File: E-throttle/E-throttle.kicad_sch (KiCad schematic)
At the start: 68 parts, among them IC1 BTS441TG, J1 Conn_01x15_Socket, J2 Conn_01x15_Socket, J3 Conn_01x11, J4 Conn_01x11, J5 776087-1, J9 Micro_SD_Card, Q1 NMOS, SW1 SW_Push, U1 74HC123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

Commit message: Changed Stepper motor driver headers to female headers
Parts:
- J3, J4: footprint Connector_PinHeader_2.54mm:PinHeader_1x11_P2.54mm_Vertical -> Connector_PinSocket_2.54mm:PinSocket_1x11_P2.54mm_Vertical

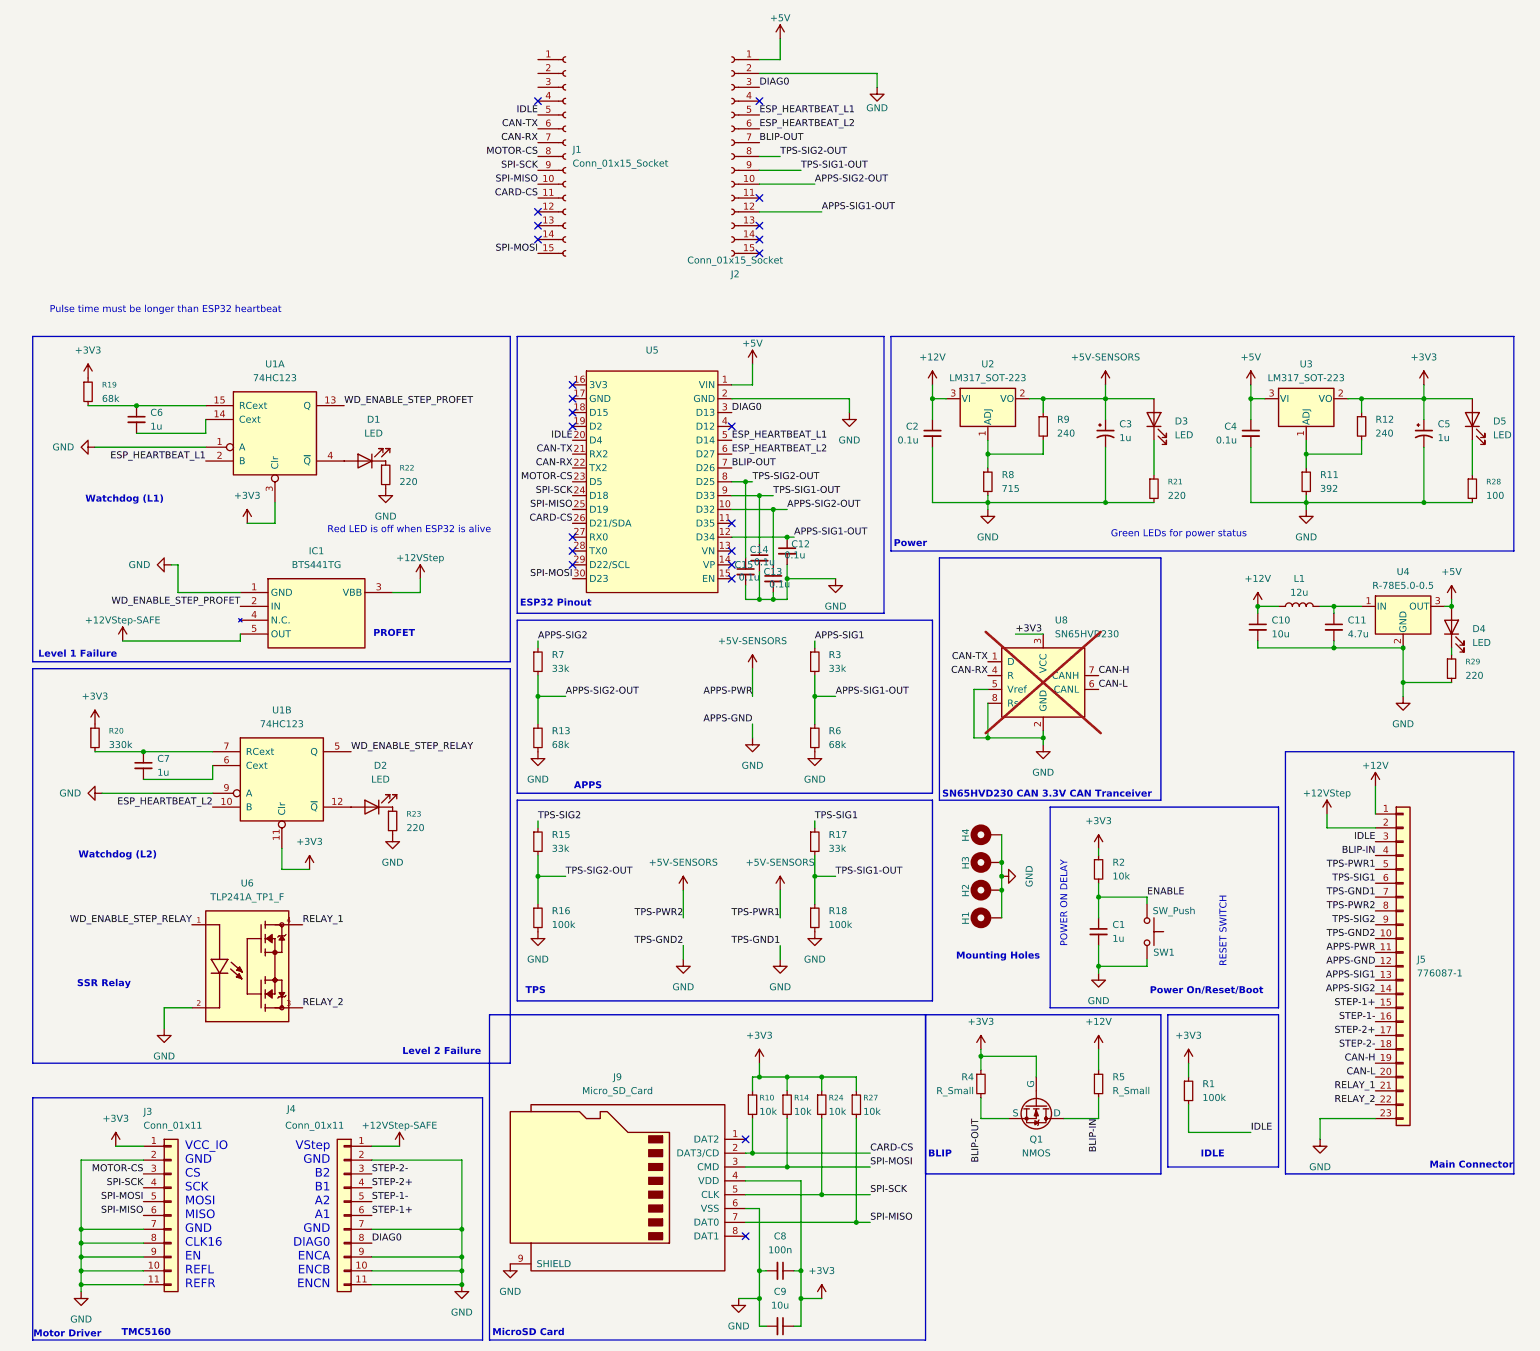
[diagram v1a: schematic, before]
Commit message: Deleted IDLE Control circuit
Fully disconnected IDLE control pin from loom
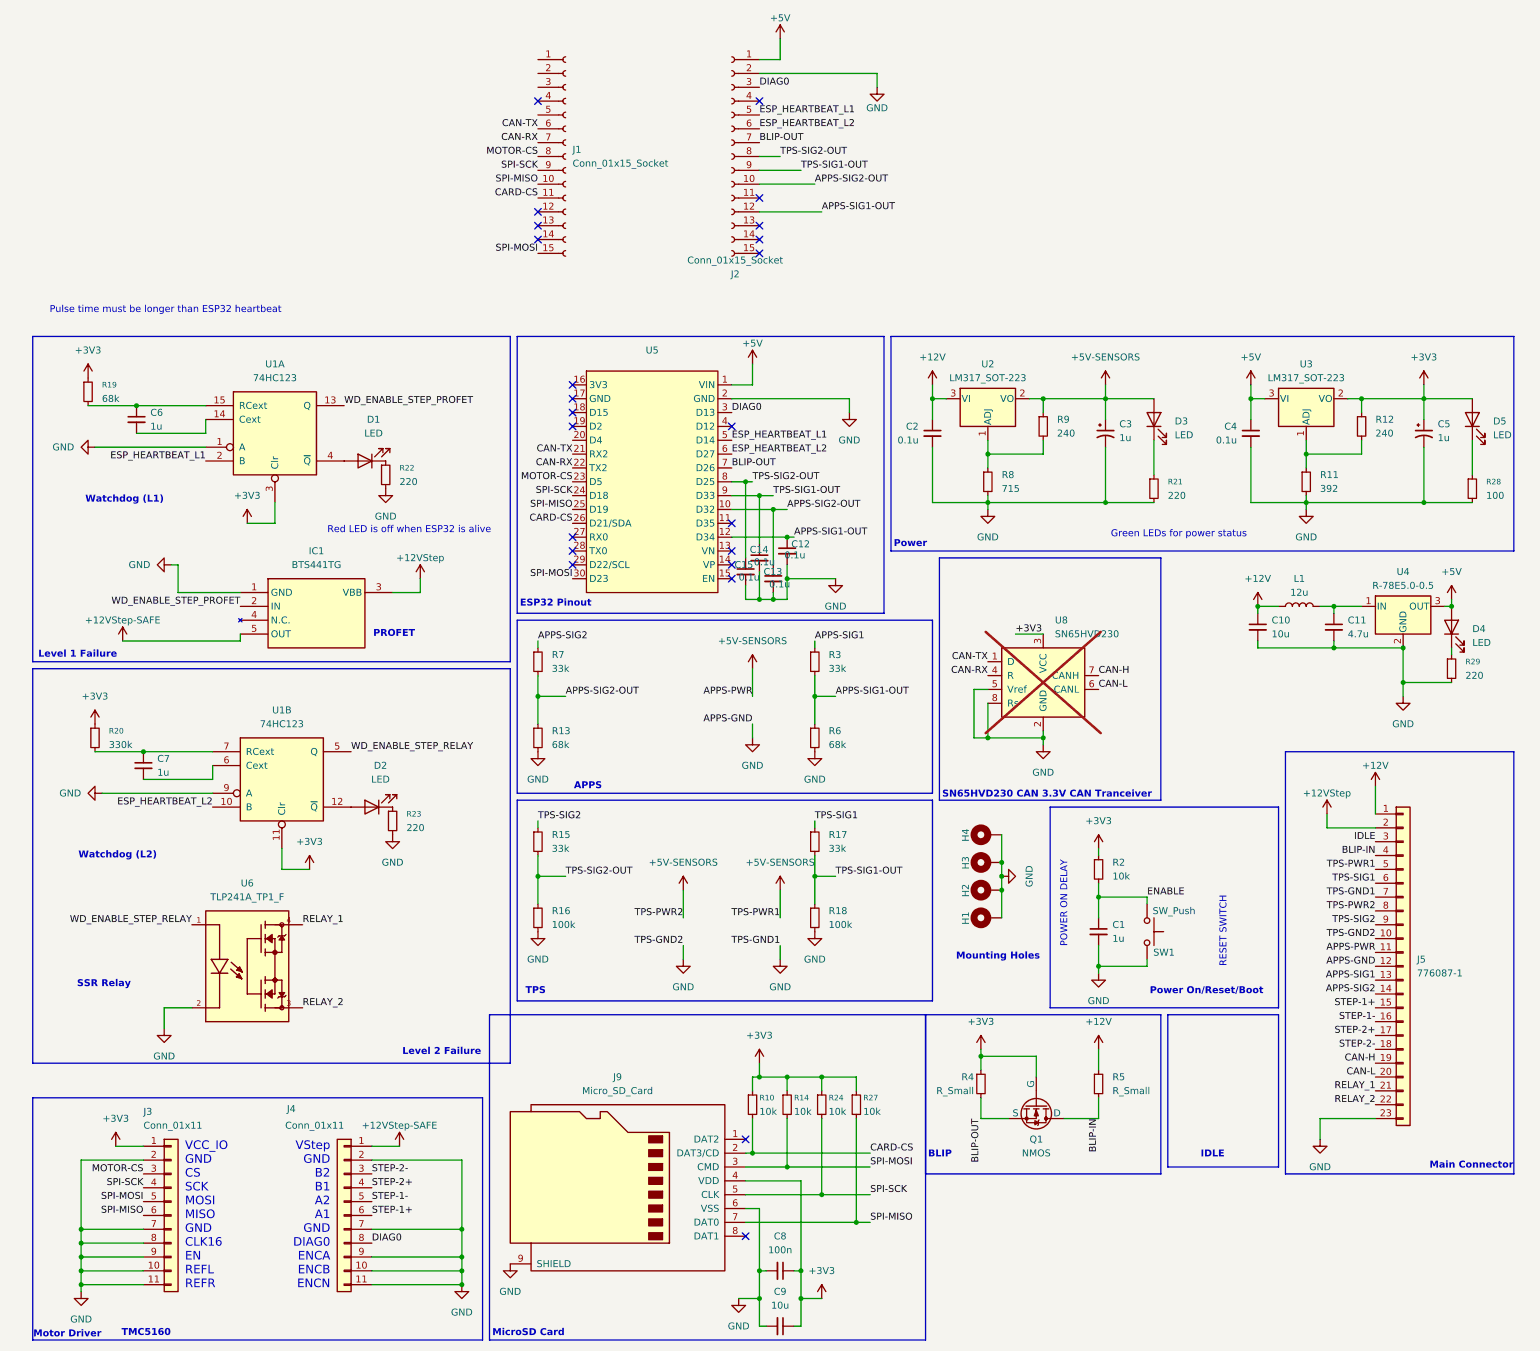
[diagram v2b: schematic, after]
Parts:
- removed R1: 100k, Resistor_SMD:R_0805_2012Metric, symbol Device:R_Small
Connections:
- net IDLE: no longer J1.5 (Pin_5), U5.20 (D4)

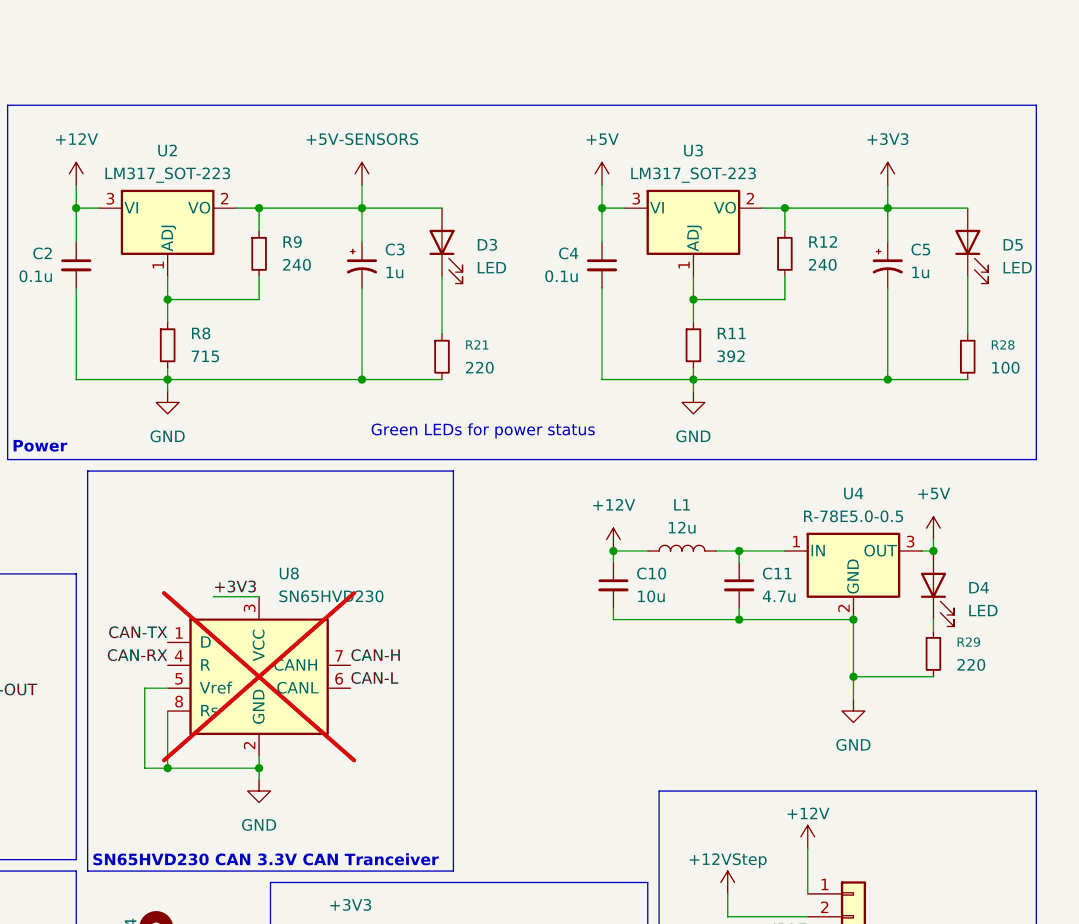
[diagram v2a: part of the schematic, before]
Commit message: changed some resistor values
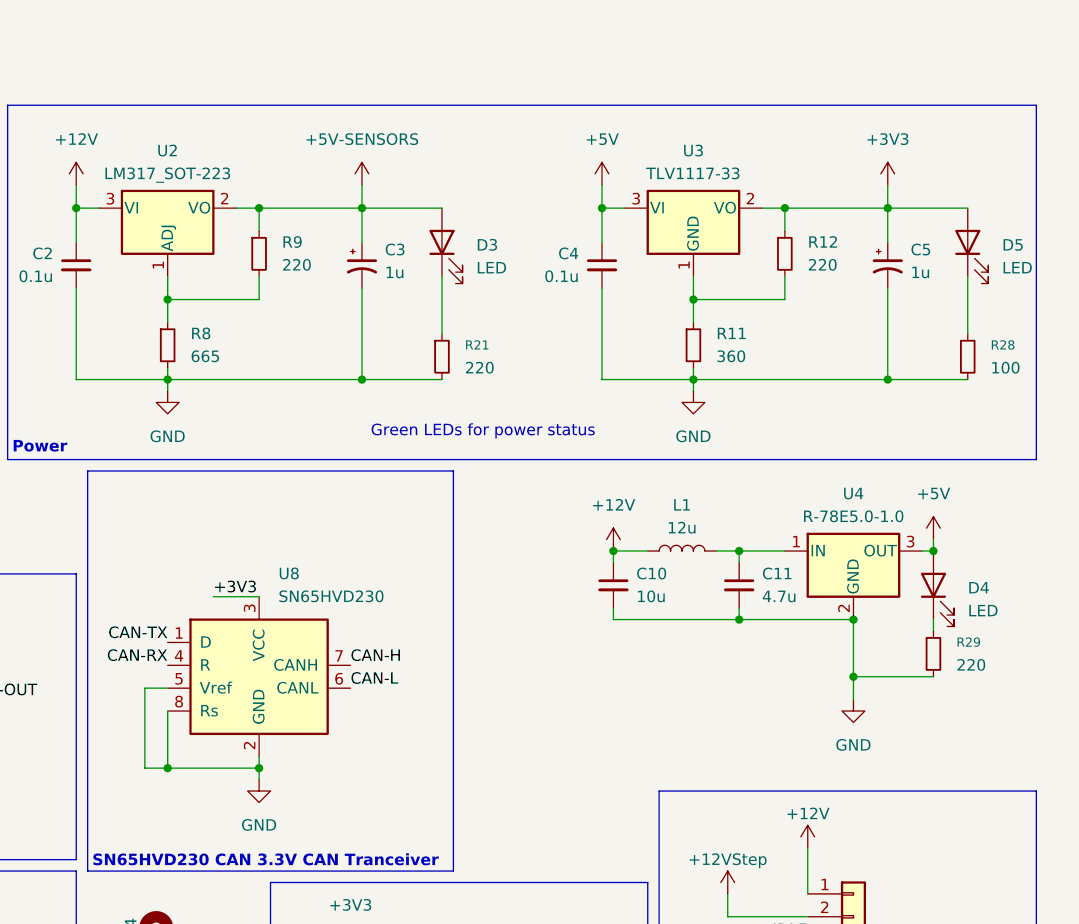
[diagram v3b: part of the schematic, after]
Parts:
- removed U3: LM317_SOT-223, Package_TO_SOT_SMD:SOT-223-3_TabPin2, symbol Regulator_Linear:LM317_SOT-223
- added U3: TLV1117-33, Package_TO_SOT_SMD:TO-252-3_TabPin2, symbol Regulator_Linear:TLV1117-33
- R11: value 392 -> 360
- R12, R9: value 240 -> 220
- R8: value 715 -> 665
- U4: value R-78E5.0-0.5 -> R-78E5.0-1.0
- U8: now fitted
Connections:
- net +3V3: now also U3.2 (VO)
- net +5V: now also U3.3 (VI)
- net at R11.1, R12.2: now also U3.1 (GND)
